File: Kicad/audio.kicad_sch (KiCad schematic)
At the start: 48 parts, among them J701 Conn_01x04, J702 Conn_02x05, J703 Conn_01x04, U701 TLV320AIC23BPW, U702 STX-4335-5BGP-S1, Y701 12M 20pF

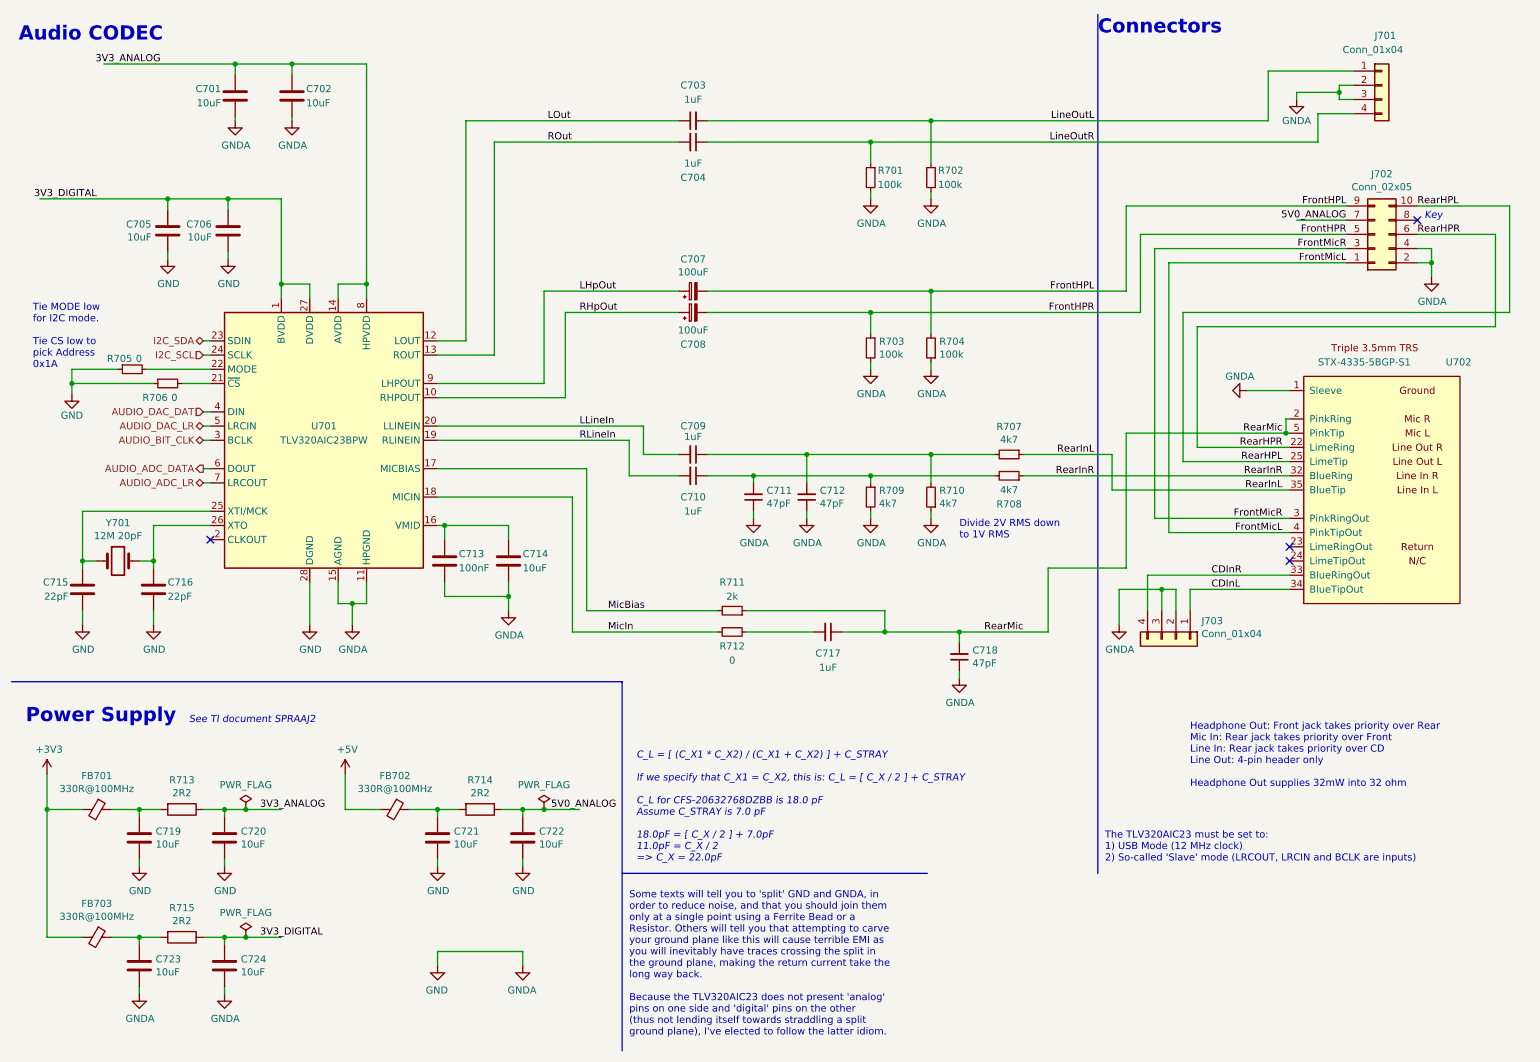
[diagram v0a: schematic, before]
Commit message: Replaced decoupling caps, and worked on PCB layout.
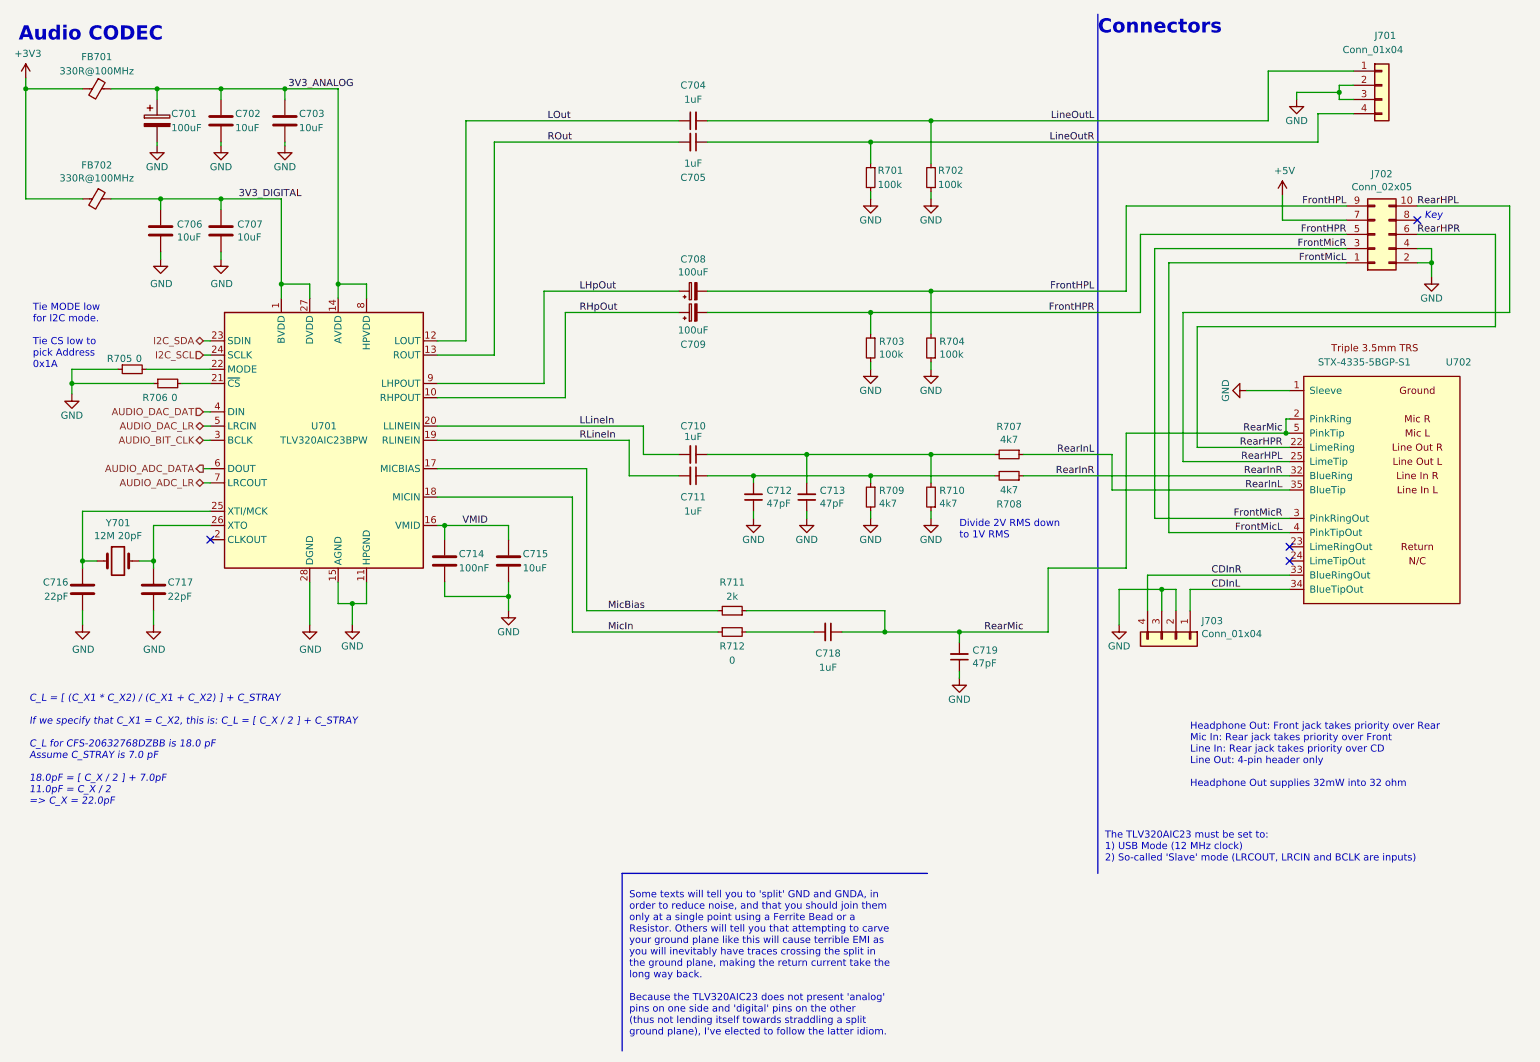
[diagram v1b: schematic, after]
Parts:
- removed C719, C720, C721, C722, C723, C724: 10uF, Capacitor_SMD:C_0805_2012Metric_Pad1.18x1.45mm_HandSolder, symbol Device:C
- removed FB702: 330R@100MHz, Inductor_SMD:L_0805_2012Metric_Pad1.15x1.40mm_HandSolder, symbol Device:FerriteBead_Small
- removed R713, R714, R715: 2R2, Resistor_SMD:R_0805_2012Metric_Pad1.20x1.40mm_HandSolder, symbol Device:R
- added C701: 100uF, Capacitor_THT:CP_Radial_D8.0mm_P5.00mm, symbol Device:C_Polarized
- C708: renamed from C707; footprint Capacitor_SMD:C_Elec_6.3x5.4 -> Capacitor_THT:CP_Radial_D8.0mm_P5.00mm; Digikey (none) -> P5182-ND; JLCPCB Collection Extended -> (none); LCSC Part# C111600 -> (none); MPN UWX1C101MCL1GB -> ECA-1HM101; Manufacturer Nichicon -> Panasonic; Mouser (none) -> 667-ECA-1HM101; Voltage 16V -> 50V
- C709: renamed from C708; footprint Capacitor_SMD:C_Elec_6.3x5.4 -> Capacitor_THT:CP_Radial_D8.0mm_P5.00mm; Digikey (none) -> P5182-ND; JLCPCB Collection Extended -> (none); LCSC Part# C111600 -> (none); MPN UWX1C101MCL1GB -> ECA-1HM101; Manufacturer Nichicon -> Panasonic; Mouser (none) -> 667-ECA-1HM101; Voltage 16V -> 50V
- renumbered C701 to C703, C703 to C704, C704 to C705, C705 to C706, C706 to C707, C709 to C710, C710 to C711, C711 to C712, C712 to C713, C713 to C714, C714 to C715, C715 to C716, C716 to C717, C717 to C718, C718 to C719, FB703 to FB702
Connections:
- net 5V0_ANALOG is gone; now on net +5V: J702.7 (Pin_7)
- net 3V3_ANALOG: now also FB701.1, C701.1
- net 3V3_DIGITAL: now also FB702.1
- net GND: now also C701.2
- net VMID: now reaches C714.1, C715.1, U701.16 (VMID)
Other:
- note removed: "Power Supply"
- note removed: "See TI document SPRAAJ2"
- moved on the sheet: C702, C703, C706, C707, FB701, FB702

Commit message: Added source resistors on SPI bus.
Also renumbered pages.
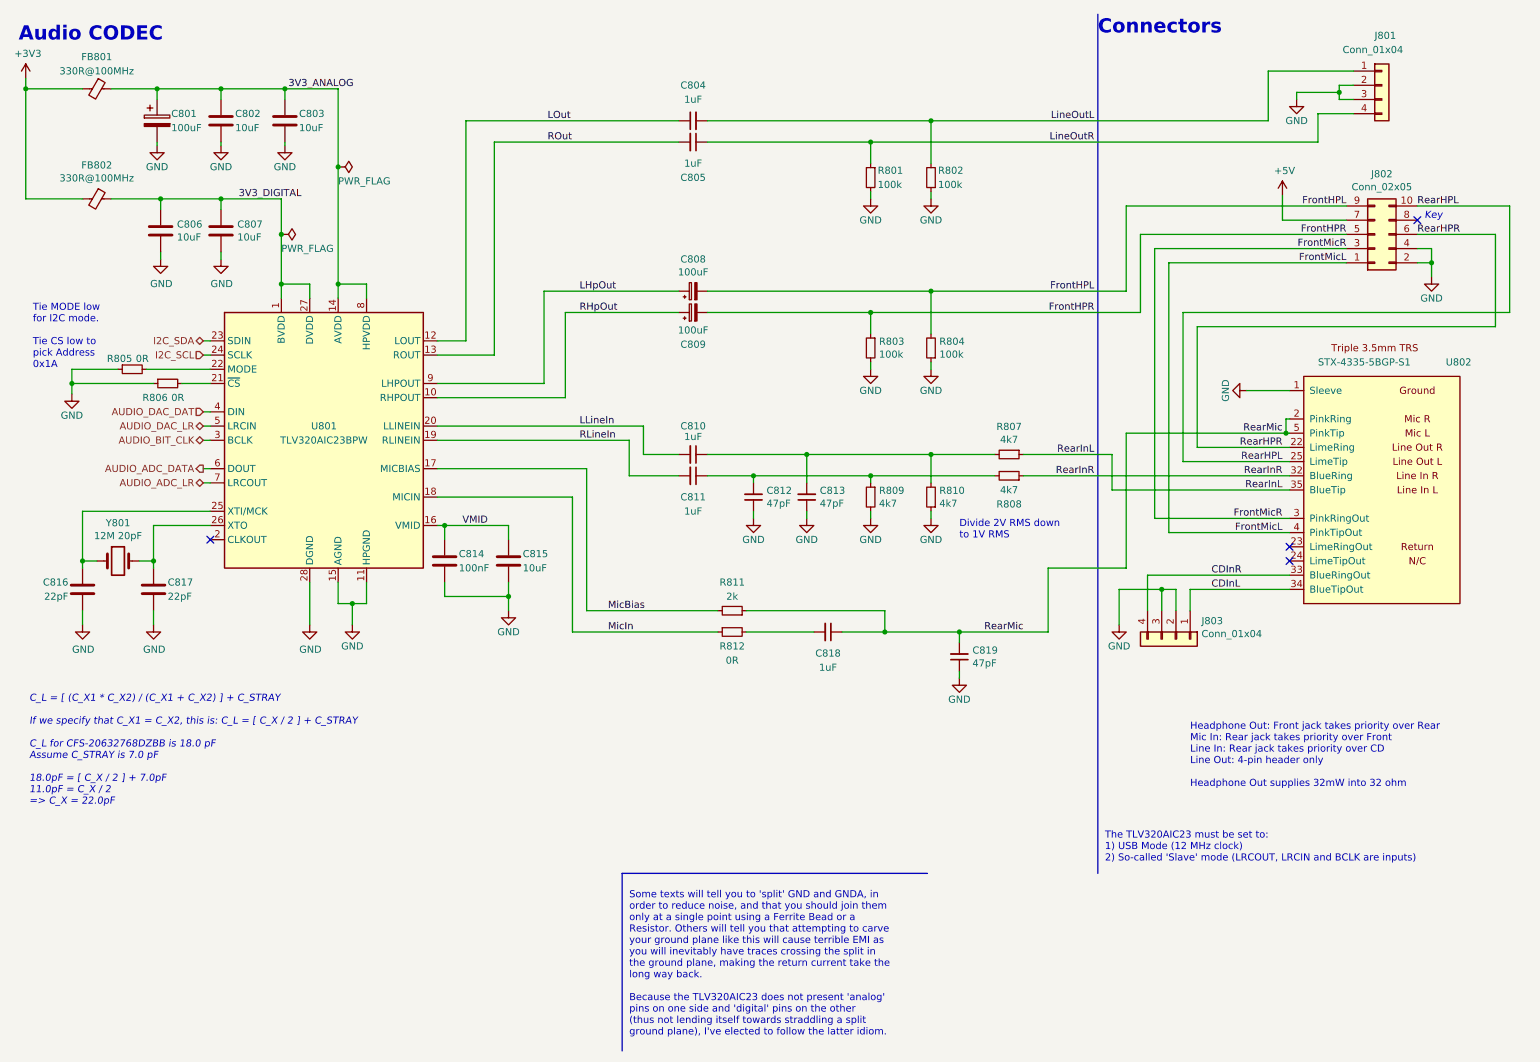
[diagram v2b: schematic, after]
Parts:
- R805: renamed from R705; value 0 -> 0R
- R806: renamed from R706; value 0 -> 0R
- R812: renamed from R712; value 0 -> 0R
- renumbered C701 to C801, C702 to C802, C703 to C803, C704 to C804, C705 to C805, C706 to C806, C707 to C807, C708 to C808, C709 to C809, C710 to C810, C711 to C811, C712 to C812, C713 to C813, C714 to C814, C715 to C815, C716 to C816, C717 to C817, C718 to C818, C719 to C819, FB701 to FB801, FB702 to FB802, J701 to J801, J702 to J802, J703 to J803, R701 to R801, R702 to R802, R703 to R803, R704 to R804, R707 to R807, R708 to R808, R709 to R809, R710 to R810, R711 to R811, U701 to U801, U702 to U802, Y701 to Y801

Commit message: Change LCSC part number on 1uF 0805s back to a Ceramic 0805.
Was a Nichicon Electrolytic, but the footprint was 0805.
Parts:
- C804, C805, C810, C811, C818: LCSC Part# C445065 -> C28323
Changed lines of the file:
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@@
       (effects (font (size 1.27 1.27)) hide)
     )
-    (property "LCSC Part#" "C445065" (id 8) (at 158.75 123.19 0)
+    (property "LCSC Part#" "C28323" (id 8) (at 158.75 123.19 0)
       (effects (font (size 1.27 1.27)) hide)
     )
@@
       (effects (font (size 1.27 1.27)) hide)
     )
-    (property "LCSC Part#" "C445065" (id 8) (at 134.62 95.25 0)
+    (property "LCSC Part#" "C28323" (id 8) (at 134.62 95.25 0)
       (effects (font (size 1.27 1.27)) hide)
     )
@@
       (effects (font (size 1.27 1.27)) hide)
     )
-    (property "LCSC Part#" "C445065" (id 8) (at 134.62 35.56 0)
+    (property "LCSC Part#" "C28323" (id 8) (at 134.62 35.56 0)
       (effects (font (size 1.27 1.27)) hide)
     )
@@
       (effects (font (size 1.27 1.27)) hide)
     )
-    (property "LCSC Part#" "C445065" (id 8) (at 134.62 91.44 0)
+    (property "LCSC Part#" "C28323" (id 8) (at 134.62 91.44 0)
       (effects (font (size 1.27 1.27)) hide)
     )
@@
       (effects (font (size 1.27 1.27)) hide)
     )
-    (property "LCSC Part#" "C445065" (id 8) (at 134.62 31.75 0)
-      (effects (font (size 1.27 1.27)) hide)
-    )
+    (property "LCSC Part#" "C28323" (id 8) (at 134.62 31.75 0)
+      (effects (font (size 1.27 1.27)) hide)
+    )

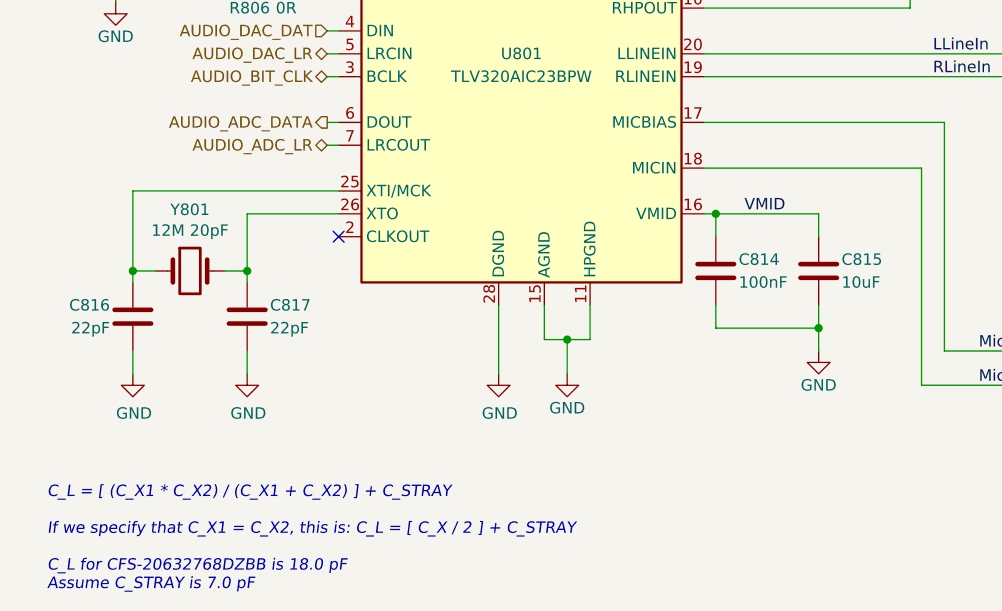
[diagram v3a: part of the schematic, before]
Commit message: Change 12M audio crystal.
Adjusted 5V fill around PSU output.
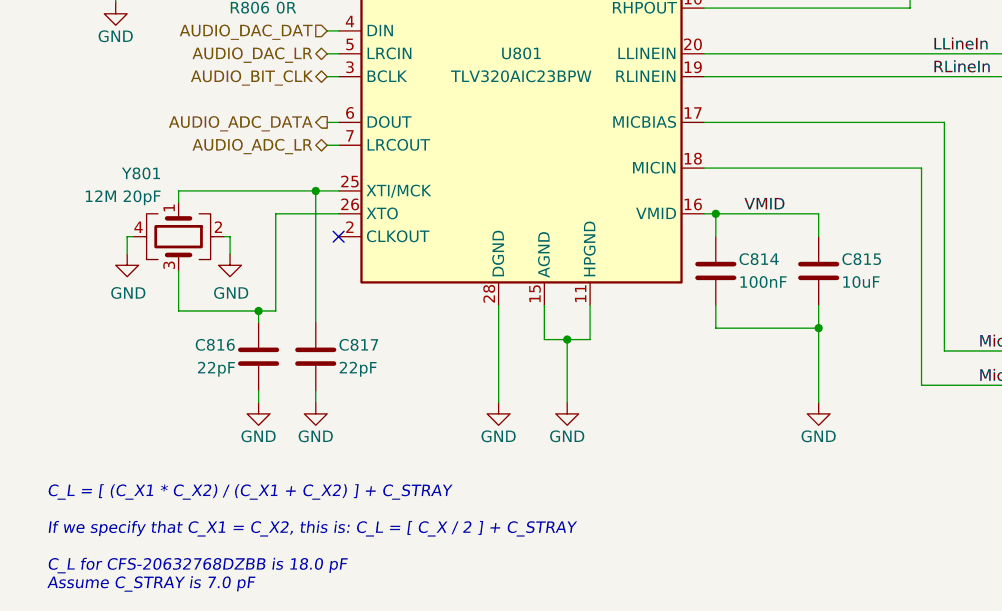
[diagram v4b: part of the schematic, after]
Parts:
- Y801: footprint Crystal:Crystal_SMD_5032-2Pin_5.0x3.2mm_HandSoldering -> Crystal:Crystal_SMD_3225-4Pin_3.2x2.5mm_HandSoldering; symbol Device:Crystal -> Device:Crystal_GND24; JLCPCB Collection Extended -> Basic; LCSC Part# C90883 -> C9002; MPN 7A12000009 -> X322512MSB4SI; Manufacturer TXC -> Yangxing Tech
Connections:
- net GND: now also Y801.2, Y801.4
- net at U801.25 (XTI/MCK), Y801.1: now also C817.1; no longer C816.2
- new net: C816.2, U801.26 (XTO), Y801.3
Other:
- moved on the sheet: C816, C817

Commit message: Set headers as DNF=0. We expect people to fit them.
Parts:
- J801, J802, J803: DNP 1 -> 0
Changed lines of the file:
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@@
       (effects (font (size 1.27 1.27)) hide)
     )
-    (property "DNP" "1" (id 4) (at 256.54 52.07 0)
+    (property "DNP" "0" (id 4) (at 256.54 52.07 0)
       (effects (font (size 1.27 1.27)) hide)
     )
@@
       (effects (font (size 1.27 1.27)) hide)
     )
-    (property "DNP" "1" (id 4) (at 220.98 124.46 0)
+    (property "DNP" "0" (id 4) (at 220.98 124.46 0)
       (effects (font (size 1.27 1.27)) hide)
     )
@@
       (effects (font (size 1.27 1.27)) hide)
     )
-    (property "DNP" "1" (id 4) (at 257.81 25.4 0)
+    (property "DNP" "0" (id 4) (at 257.81 25.4 0)
       (effects (font (size 1.27 1.27)) hide)
     )
